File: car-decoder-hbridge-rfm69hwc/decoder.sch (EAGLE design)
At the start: 50 parts, among them U1 RFM69HCW, U3 MCP73831, U4 ATMEGA328P, U6 MIC5219 3.3V, Y1 16MHZ

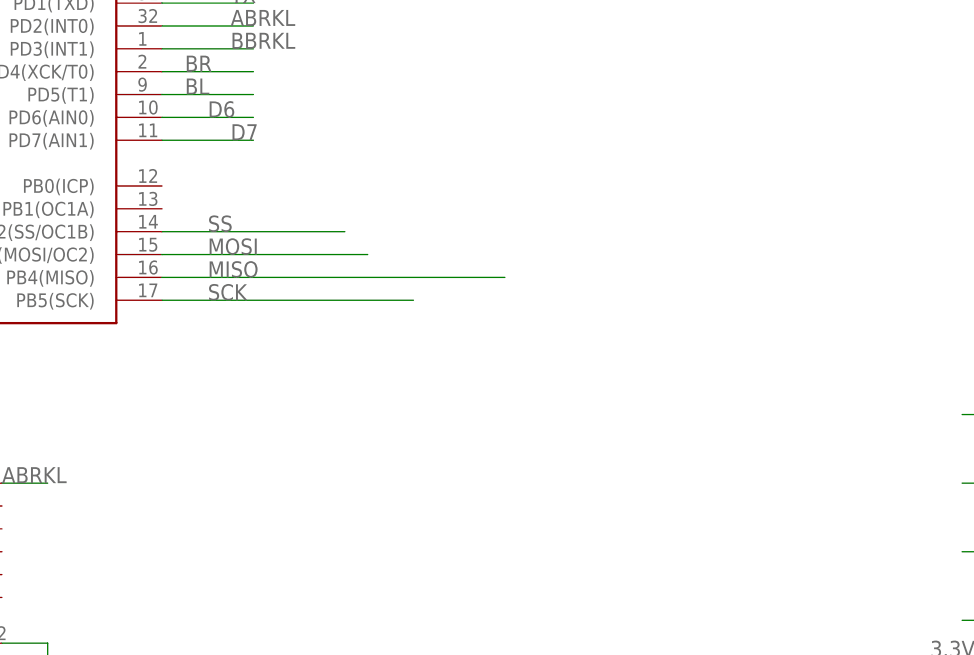
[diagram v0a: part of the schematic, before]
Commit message: Fix boards and add the pi control station
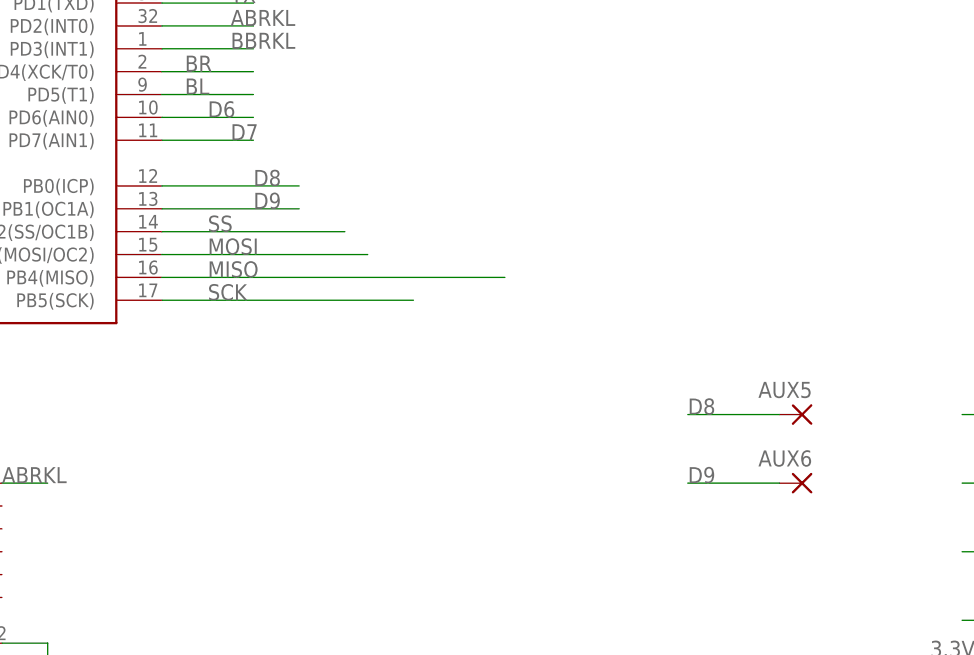
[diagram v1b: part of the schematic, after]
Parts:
- added AUX5, AUX6: (no value), wirepad:SMD2
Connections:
- new net D8: AUX5.P, U4.PB0(ICP)
- new net D9: AUX6.P, U4.PB1(OC1A)
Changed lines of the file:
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@@
 <part name="R17" library="SparkFun-Resistors" deviceset="RESISTOR" device="0603-RES" value="10k"/>
 <part name="SUPPLY2" library="SparkFun-Aesthetics" deviceset="VCC" device="" value="3.3V"/>
+<part name="AUX5" library="wirepad" deviceset="SMD2" device=""/>
+<part name="AUX6" library="wirepad" deviceset="SMD2" device=""/>
 </parts>
 <sheets>
@@
 <instance part="R17" gate="G$1" x="20.32" y="-12.7"/>
 <instance part="SUPPLY2" gate="G$1" x="22.86" y="-2.54"/>
+<instance part="AUX5" gate="1" x="149.86" y="2.54" rot="MR0"/>
+<instance part="AUX6" gate="1" x="149.86" y="-5.08" rot="MR0"/>
 </instances>
 <busses>
@@
 </segment>
 </net>
+<net name="D8" class="0">
+<segment>
+<pinref part="U4" gate="G$1" pin="PB0(ICP)"/>
+<wire x1="78.74" y1="27.94" x2="93.98" y2="27.94" width="0.1524" layer="91"/>
+<label x="88.9" y="27.94" size="1.778" layer="95"/>
+</segment>
+<segment>
+<pinref part="AUX5" gate="1" pin="P"/>
+<wire x1="147.32" y1="2.54" x2="137.16" y2="2.54" width="0.1524" layer="91"/>
+<label x="137.16" y="2.54" size="1.778" layer="95"/>
+</segment>
+</net>
+<net name="D9" class="0">
+<segment>
+<pinref part="U4" gate="G$1" pin="PB1(OC1A)"/>
+<wire x1="78.74" y1="25.4" x2="93.98" y2="25.4" width="0.1524" layer="91"/>
+<label x="88.9" y="25.4" size="1.778" layer="95"/>
+</segment>
+<segment>
+<pinref part="AUX6" gate="1" pin="P"/>
+<wire x1="147.32" y1="-5.08" x2="137.16" y2="-5.08" width="0.1524" layer="91"/>
+<label x="137.16" y="-5.08" size="1.778" layer="95"/>
+</segment>
+</net>
